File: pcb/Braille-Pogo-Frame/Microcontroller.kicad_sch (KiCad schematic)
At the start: 3 parts, among them SW1 SW_Push, SW2 SW_Push, U9 RP2040-Zero

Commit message: PCB: Update footprint assignments
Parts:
- SW1, SW2: footprint (none) -> Button_Switch_THT:SW_PUSH_6mm
- U9: footprint Braille_Display_Footprint_Lib:RP2040 Zero -> 00-lib-footprints:RP2040 Zero
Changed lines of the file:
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@@
 			)
 		)
-		(property "Footprint" "Braille_Display_Footprint_Lib:RP2040 Zero"
+		(property "Footprint" "00-lib-footprints:RP2040 Zero"
 			(at 115.57 57.658 0)
 			(effects
@@
 			)
 		)
-		(property "Footprint" ""
+		(property "Footprint" "Button_Switch_THT:SW_PUSH_6mm"
 			(at 55.88 83.82 0)
 			(effects
@@
 			)
 		)
-		(property "Footprint" ""
+		(property "Footprint" "Button_Switch_THT:SW_PUSH_6mm"
 			(at 69.85 83.82 0)
 			(effects

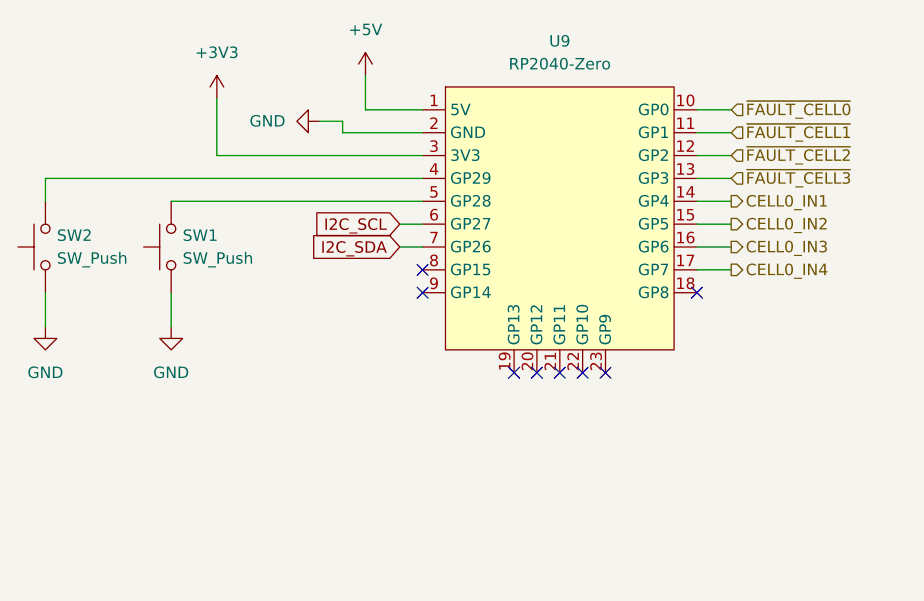
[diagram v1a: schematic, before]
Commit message: PCB: Place motor drivers and horiz. rail mounts
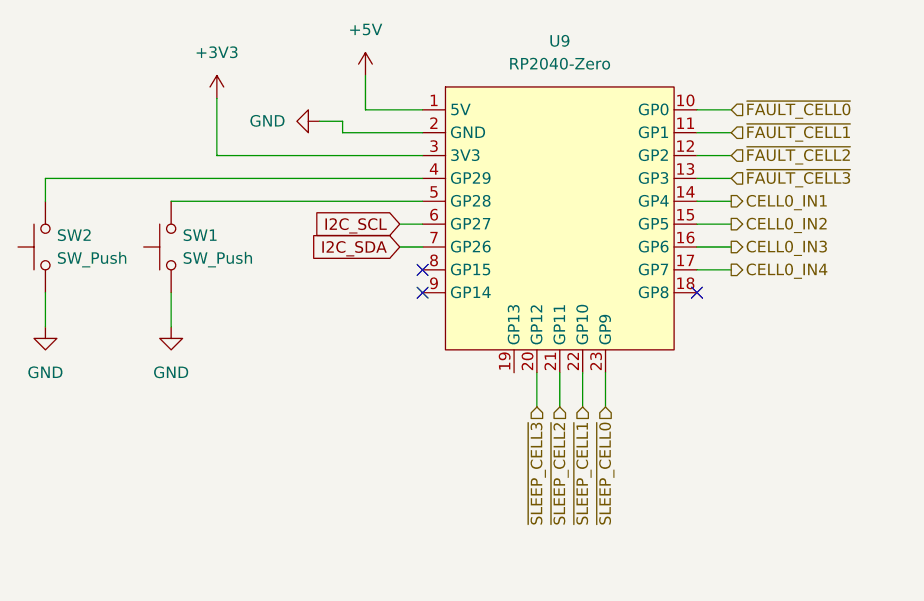
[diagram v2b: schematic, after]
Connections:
- net ~{SLEEP_CELL3}: now reaches U9.20 (GP12)
- net ~{SLEEP_CELL2}: now reaches U9.21 (GP11)
- net ~{SLEEP_CELL1}: now reaches U9.22 (GP10)
- net ~{SLEEP_CELL0}: now reaches U9.23 (GP9)
- no-connect marks 8 -> 3
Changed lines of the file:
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@@
 	(paper "USLetter")
 	(no_connect
-		(at 123.19 97.79)
-	)
-	(no_connect
-		(at 118.11 97.79)
-	)
-	(no_connect
 		(at 102.87 88.9)
-	)
-	(no_connect
-		(at 115.57 97.79)
 	)
 	(no_connect
@@
 	)
 	(no_connect
-		(at 113.03 97.79)
-	)
-	(no_connect
 		(at 133.35 88.9)
 	)
-	(no_connect
-		(at 120.65 97.79)
-	)
 	(wire
 		(pts
@@
 	(wire
 		(pts
+			(xy 120.65 101.6) (xy 120.65 97.79)
+		)
+		(stroke
+			(width 0)
+			(type default)
+		)
+	)
+	(wire
+		(pts
+			(xy 115.57 101.6) (xy 115.57 97.79)
+		)
+		(stroke
+			(width 0)
+			(type default)
+		)
+	)
+	(wire
+		(pts
 			(xy 96.52 68.58) (xy 102.87 68.58)
 		)
@@
 	(wire
 		(pts
+			(xy 118.11 101.6) (xy 118.11 97.79)
+		)
+		(stroke
+			(width 0)
+			(type default)
+		)
+	)
+	(wire
+		(pts
 			(xy 133.35 71.12) (xy 137.16 71.12)
 		)
@@
 		(pts
 			(xy 133.35 83.82) (xy 137.16 83.82)
+		)
+		(stroke
+			(width 0)
+			(type default)
+		)
+	)
+	(wire
+		(pts
+			(xy 123.19 101.6) (xy 123.19 97.79)
 		)
 		(stroke
@@
 		)
 	)
+	(hierarchical_label "~{SLEEP_CELL0}"
+		(shape input)
+		(at 123.19 101.6 270)
+		(fields_autoplaced yes)
+		(effects
+			(font
+				(size 1.27 1.27)
+			)
+			(justify right)
+		)
+	)
 	(hierarchical_label "CELL0_IN4"
 		(shape output)
@@
 		)
 	)
+	(hierarchical_label "~{SLEEP_CELL3}"
+		(shape input)
+		(at 115.57 101.6 270)
+		(fields_autoplaced yes)
+		(effects
+			(font
+				(size 1.27 1.27)
+			)
+			(justify right)
+		)
+	)
 	(hierarchical_label "~{FAULT_CELL2}"
 		(shape input)
@@
 		)
 	)
+	(hierarchical_label "~{SLEEP_CELL1}"
+		(shape input)
+		(at 120.65 101.6 270)
+		(fields_autoplaced yes)
+		(effects
+			(font
+				(size 1.27 1.27)
+			)
+			(justify right)
+		)
+	)
 	(hierarchical_label "~{FAULT_CELL3}"
 		(shape input)
@@
 		)
 	)
+	(hierarchical_label "~{SLEEP_CELL2}"
+		(shape input)
+		(at 118.11 101.6 270)
+		(fields_autoplaced yes)
+		(effects
+			(font
+				(size 1.27 1.27)
+			)
+			(justify right)
+		)
+	)
